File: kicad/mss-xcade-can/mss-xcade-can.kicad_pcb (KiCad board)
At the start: 2 copper layers, 38.1 x 35.6 mm, 12 parts, among them J1 Conn_02x03_Odd_Even, J2 8P8C, J3 8P8C, U1 TCAN1042

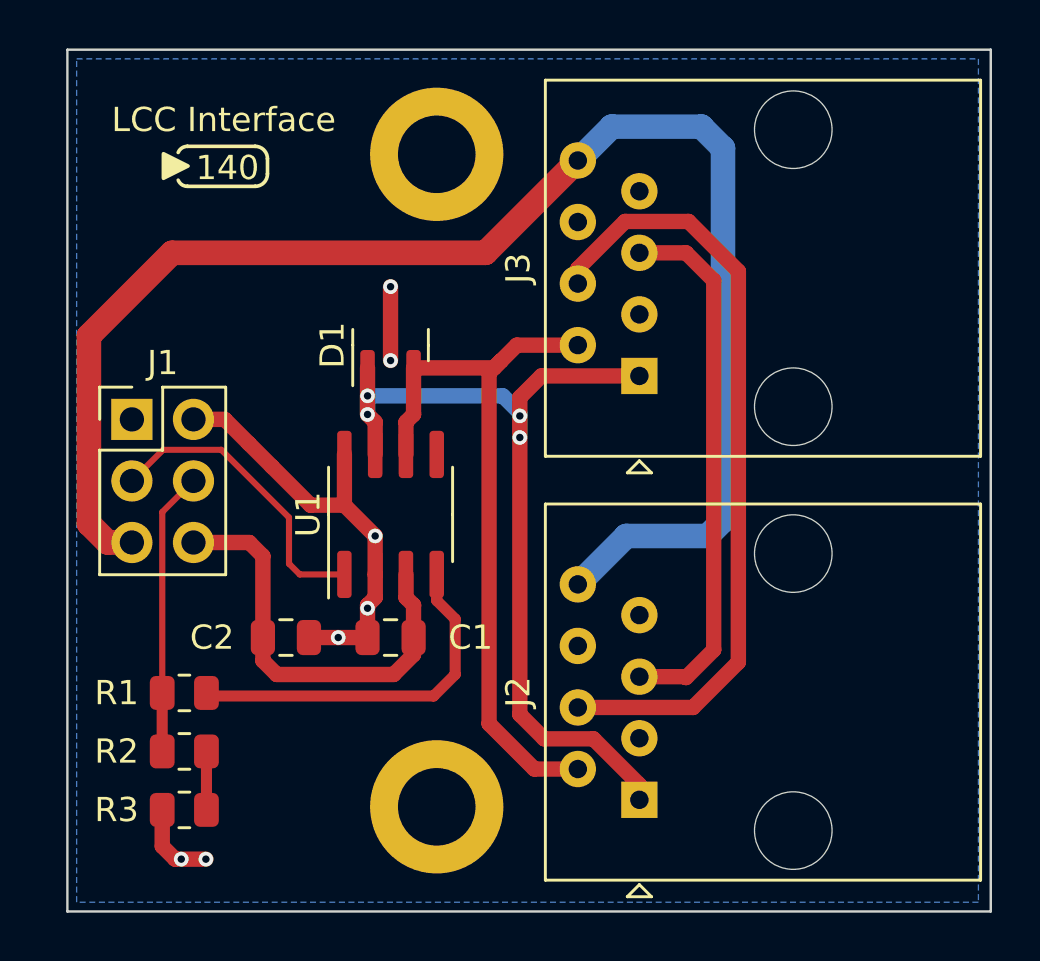
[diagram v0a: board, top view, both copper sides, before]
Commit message: Add optional termination resistor
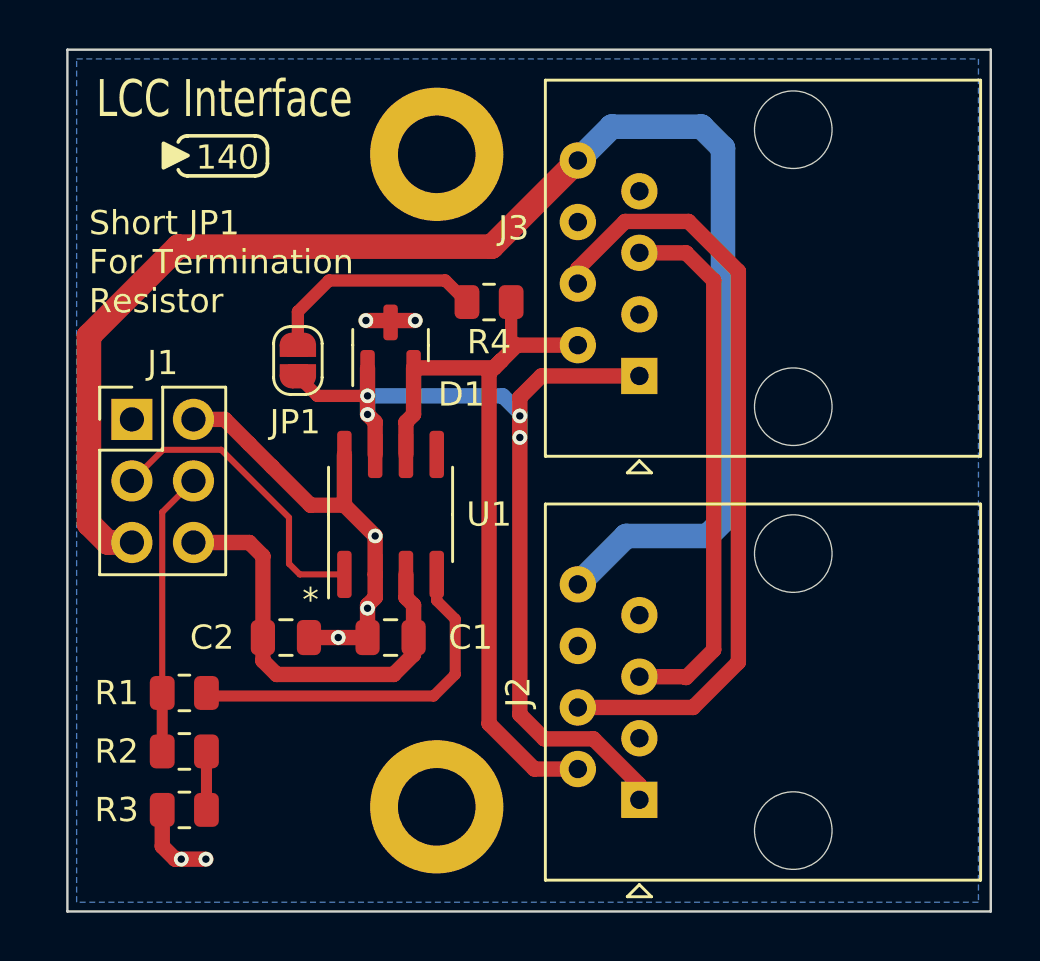
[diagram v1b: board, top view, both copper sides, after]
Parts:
- added JP1: SolderJumper_2_Open, Jumper:SolderJumper-2_P1.3mm_Open_RoundedPad1.0x1.5mm, F.Cu at (85.7, 127.1)
- added R4: 120, Resistor_SMD:R_0805_2012Metric, F.Cu at (93.6, 124.7)
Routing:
- net Net-(JP1-Pad2): track 0.00 -> 9.24 mm
- net Net-(D1-Pad1): track 37.2 -> 40.4 mm
- net Net-(D1-Pad2): track 30.5 -> 32.4 mm
- net GND: track 24.9 -> 23.9 mm
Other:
- board text added: "*"
- board text added: "Short JP1 For Termination Resistor"
